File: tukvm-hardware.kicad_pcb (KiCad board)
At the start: 2 copper layers, 115.8 x 68.9 mm, 137 parts, among them J1 PCIexpress_x1, J2 PCIexpress_bracket, J3 HDMI_A, J4 USB_C_Receptacle_USB2.0, J5 Conn_02x08_Odd_Even, J6 USB_9P, J7 Conn_01x04, J8 RS232_MALE, SW1 SKRK, SW3 TS-1187A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

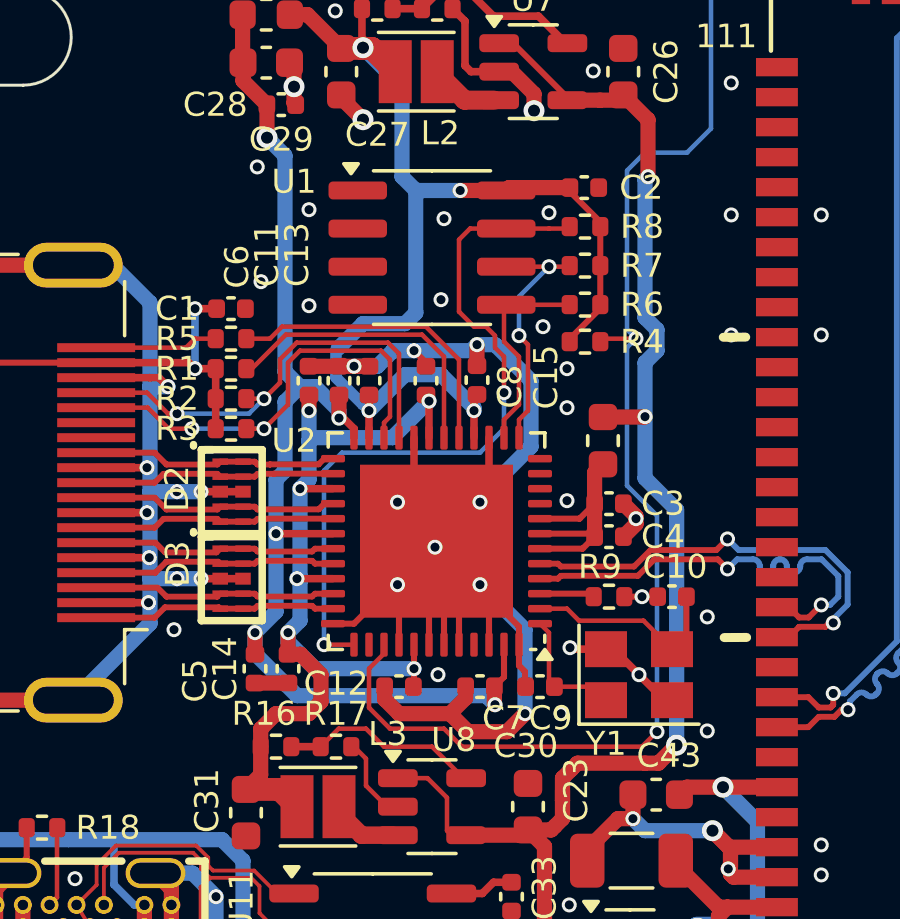
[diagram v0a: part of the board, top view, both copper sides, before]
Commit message: Fix MS2109 symbol power pins, initial v1 release
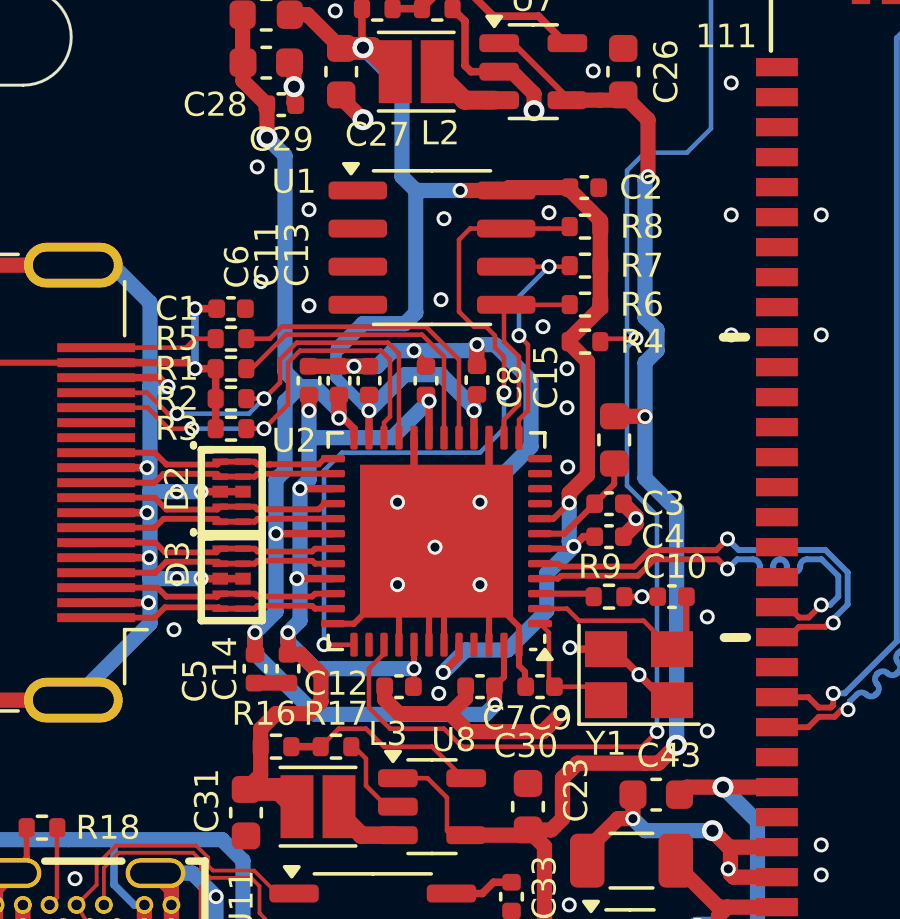
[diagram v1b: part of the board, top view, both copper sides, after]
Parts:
- moved FB1 0.38 mm to (92.1, 144.3)
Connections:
- C4 pad 2: V33USB -> MS_3V3
- U2 pad 44: Earth -> MS_3V3
- U2 pad 6: V33USB -> MS_3V3
- U2 pad 8: V33USB -> MS_3V3
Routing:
- net MS_3V3: track 40.1 -> 58.6 mm, vias 4 -> 7
- net Earth: track 275.5 -> 270.3 mm, vias 140 -> 139
- net V33USB: track 8.40 -> 3.84 mm

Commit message: Fix OTG USB polarity
Signed-off-by: Yichuan Gao <gaoyichuan000@gmail.com>
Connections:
- J6 pad 5: unconnected-(J6-P1_D+-Pad5) -> /OTG_D+
- J6 pad 6: /OTG_D- -> unconnected-(J6-P2_D+-Pad6)
- J6 pad 7: unconnected-(J6-P1_D--Pad7) -> /OTG_D-
- J6 pad 8: /OTG_D+ -> unconnected-(J6-P2_D--Pad8)
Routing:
- net /OTG_D+: track 108.1 -> 98.4 mm
- net /OTG_D-: track 108.0 -> 99.2 mm
